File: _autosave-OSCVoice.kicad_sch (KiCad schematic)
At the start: 38 parts, among them U10 TL074, U9 SSI2131

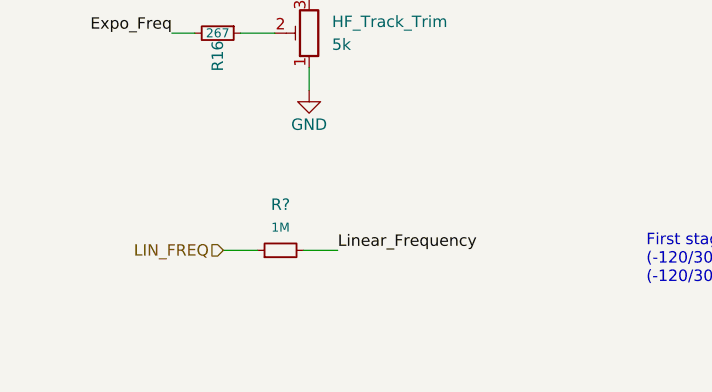
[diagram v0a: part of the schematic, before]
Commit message: Updates to linear frequency controls
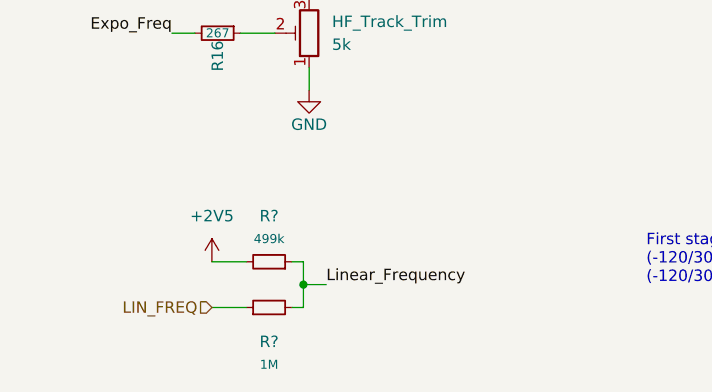
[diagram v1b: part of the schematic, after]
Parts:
- added R?: 499k, Resistor_SMD:R_0805_2012Metric, symbol Device:R_Small
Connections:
- net +2V5: now also R?.2
- net Linear_Frequency: now also R?.1
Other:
- moved on the sheet: R?
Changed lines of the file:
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@@
   (junction (at 125.73 39.37) (diameter 0) (color 0 0 0 0)
   )
+  (junction (at 54.61 158.75) (diameter 0) (color 0 0 0 0)
+  )
   (junction (at 172.72 140.97) (diameter 0) (color 0 0 0 0)
   )
@@
     (stroke (width 0) (type default) (color 0 0 0 0))
   )
-  (wire (pts (xy 54.61 154.94) (xy 58.42 154.94))
+  (wire (pts (xy 53.34 161.29) (xy 54.61 161.29))
+    (stroke (width 0) (type default) (color 0 0 0 0))
+  )
+  (wire (pts (xy 54.61 158.75) (xy 54.61 156.21))
     (stroke (width 0) (type default) (color 0 0 0 0))
   )
@@
     (stroke (width 0) (type default) (color 0 0 0 0))
   )
+  (wire (pts (xy 48.26 156.21) (xy 44.45 156.21))
+    (stroke (width 0) (type default) (color 0 0 0 0))
+  )
   (wire (pts (xy 180.34 30.48) (xy 185.42 30.48))
     (stroke (width 0) (type default) (color 0 0 0 0))
@@
     (stroke (width 0) (type default) (color 0 0 0 0))
   )
-  (wire (pts (xy 45.72 154.94) (xy 49.53 154.94))
+  (wire (pts (xy 44.45 161.29) (xy 48.26 161.29))
     (stroke (width 0) (type default) (color 0 0 0 0))
   )
@@
     (stroke (width 0) (type default) (color 0 0 0 0))
   )
+  (wire (pts (xy 54.61 161.29) (xy 54.61 158.75))
+    (stroke (width 0) (type default) (color 0 0 0 0))
+  )
   (wire (pts (xy 177.165 48.26) (xy 180.34 48.26))
     (stroke (width 0) (type default) (color 0 0 0 0))
@@
     (stroke (width 0) (type default) (color 0 0 0 0))
   )
+  (wire (pts (xy 54.61 156.21) (xy 53.34 156.21))
+    (stroke (width 0) (type default) (color 0 0 0 0))
+  )
   (wire (pts (xy 63.5 64.77) (xy 64.77 64.77))
     (stroke (width 0) (type default) (color 0 0 0 0))
@@
   )
   (wire (pts (xy 125.73 44.45) (xy 125.73 39.37))
+    (stroke (width 0) (type default) (color 0 0 0 0))
+  )
+  (wire (pts (xy 54.61 158.75) (xy 57.15 158.75))
     (stroke (width 0) (type default) (color 0 0 0 0))
   )
@@
     (effects (font (size 1.27 1.27)) (justify right bottom))
   )
-  (label "Linear_Frequency" (at 58.42 154.94 0)
+  (label "Linear_Frequency" (at 57.15 158.75 0)
     (effects (font (size 1.27 1.27)) (justify left bottom))
   )
@@
     (effects (font (size 1.27 1.27)) (justify right))
   )
-  (hierarchical_label "LIN_FREQ" (shape input) (at 45.72 154.94 180)
+  (hierarchical_label "LIN_FREQ" (shape input) (at 44.45 161.29 180)
     (effects (font (size 1.27 1.27)) (justify right))
   )
@@
   (hierarchical_label "Hard_Synch_Switch" (shape input) (at 258.445 22.225 180)
     (effects (font (size 1.27 1.27)) (justify right))
+  )
+  (symbol (lib_id "power:+2V5") (at 44.45 156.21 0) (mirror y) (unit 1)
+    (in_bom yes) (on_board yes) (fields_autoplaced)
+    (property "Reference" "#PWR?" (id 0) (at 44.45 160.02 0)
+      (effects (font (size 1.27 1.27)) hide)
+    )
+    (property "Value" "+2V5" (id 1) (at 44.45 151.13 0))
+    (property "Footprint" "" (id 2) (at 44.45 156.21 0)
+      (effects (font (size 1.27 1.27)) hide)
+    )
+    (property "Datasheet" "" (id 3) (at 44.45 156.21 0)
+      (effects (font (size 1.27 1.27)) hide)
+    )
+    (pin "1")
   )
   (symbol (lib_id "Device:R_Small") (at 174.625 30.48 270) (unit 1)
@@
     )
     (property "Datasheet" "~" (id 3) (at 45.085 130.81 0)
+      (effects (font (size 1.27 1.27)) hide)
+    )
+    (pin "1")
+    (pin "2")
+  )
+  (symbol (lib_id "Device:R_Small") (at 50.8 156.21 270) (mirror x) (unit 1)
+    (in_bom yes) (on_board yes) (fields_autoplaced)
+    (property "Reference" "R?" (id 0) (at 50.8 151.13 90))
+    (property "Value" "499k" (id 1) (at 50.8 153.67 90)
+      (effects (font (size 1 1)))
+    )
+    (property "Footprint" "Resistor_SMD:R_0805_2012Metric" (id 2) (at 50.8 156.21 0)
+      (effects (font (size 1.27 1.27)) hide)
+    )
+    (property "Datasheet" "~" (id 3) (at 50.8 156.21 0)
       (effects (font (size 1.27 1.27)) hide)
     )
@@
     (pin "2")
   )
-  (symbol (lib_id "Device:R_Small") (at 52.07 154.94 90) (unit 1)
+  (symbol (lib_id "Device:R_Small") (at 50.8 161.29 90) (unit 1)
     (in_bom yes) (on_board yes) (fields_autoplaced)
-    (property "Reference" "R?" (id 0) (at 52.07 149.86 90))
-    (property "Value" "1M" (id 1) (at 52.07 152.4 90)
+    (property "Reference" "R?" (id 0) (at 50.8 165.1 90))
+    (property "Value" "1M" (id 1) (at 50.8 167.64 90)
       (effects (font (size 1 1)))
     )
-    (property "Footprint" "Resistor_SMD:R_0805_2012Metric" (id 2) (at 52.07 154.94 0)
-      (effects (font (size 1.27 1.27)) hide)
-    )
-    (property "Datasheet" "~" (id 3) (at 52.07 154.94 0)
-      (effects (font (size 1.27 1.27)) hide)
-    )
+    (property "Footprint" "Resistor_SMD:R_0805_2012Metric" (id 2) (at 50.8 161.29 0)
+      (effects (font (size 1.27 1.27)) hide)
+    )
+    (property "Datasheet" "~" (id 3) (at 50.8 161.29 0)
+      (effects (font (size 1.27 1.27)) hide)
+    )
